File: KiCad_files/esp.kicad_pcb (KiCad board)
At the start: 2 copper layers, 86 x 75 mm, 69 parts, among them J1 Conn_01x02_Pin, J2 USB4105-GF-A, J3 Conn_01x16_Pin, Q2 DMP3099L, SW1 SLW-171175-7A-N-D, U1 B3U-1000P, U12 ESP32-S3-MINI-1U, U13 BNO085, U2 1060, U7 LTC4412xS6

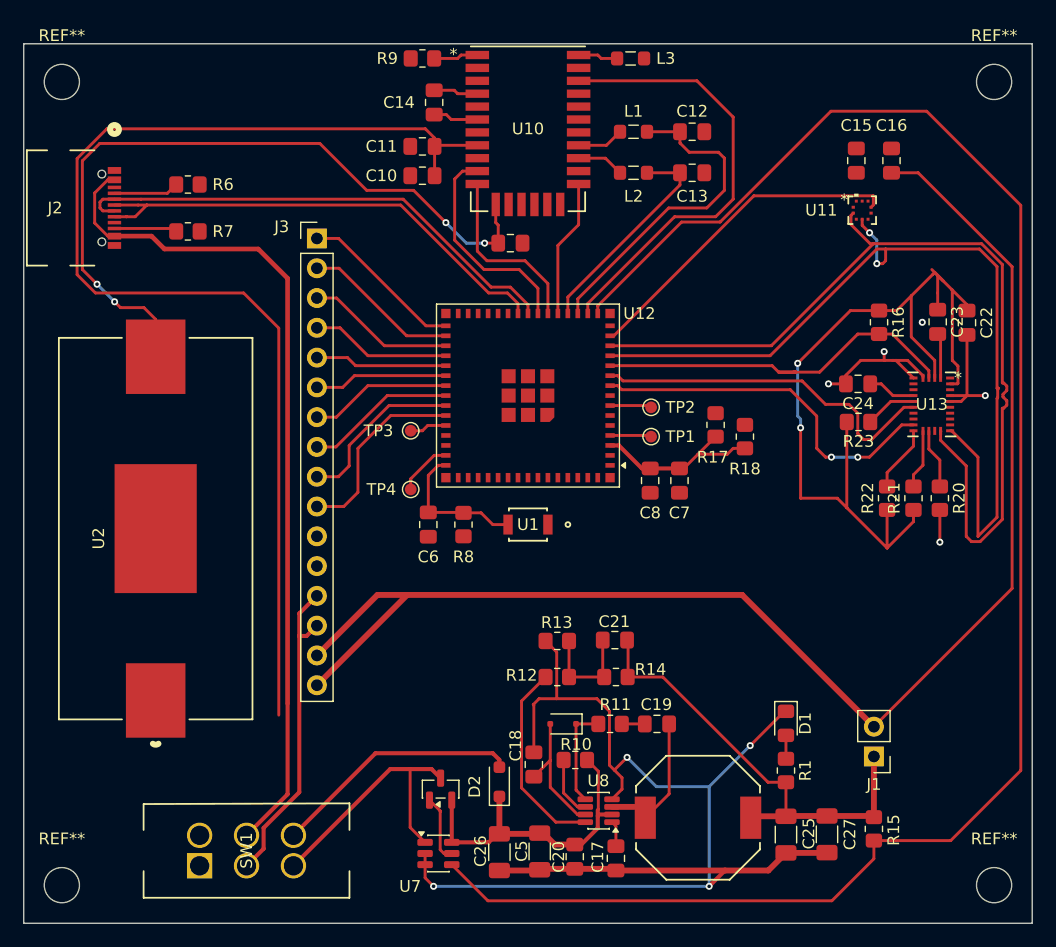
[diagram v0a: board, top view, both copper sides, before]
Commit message: backside GND fill
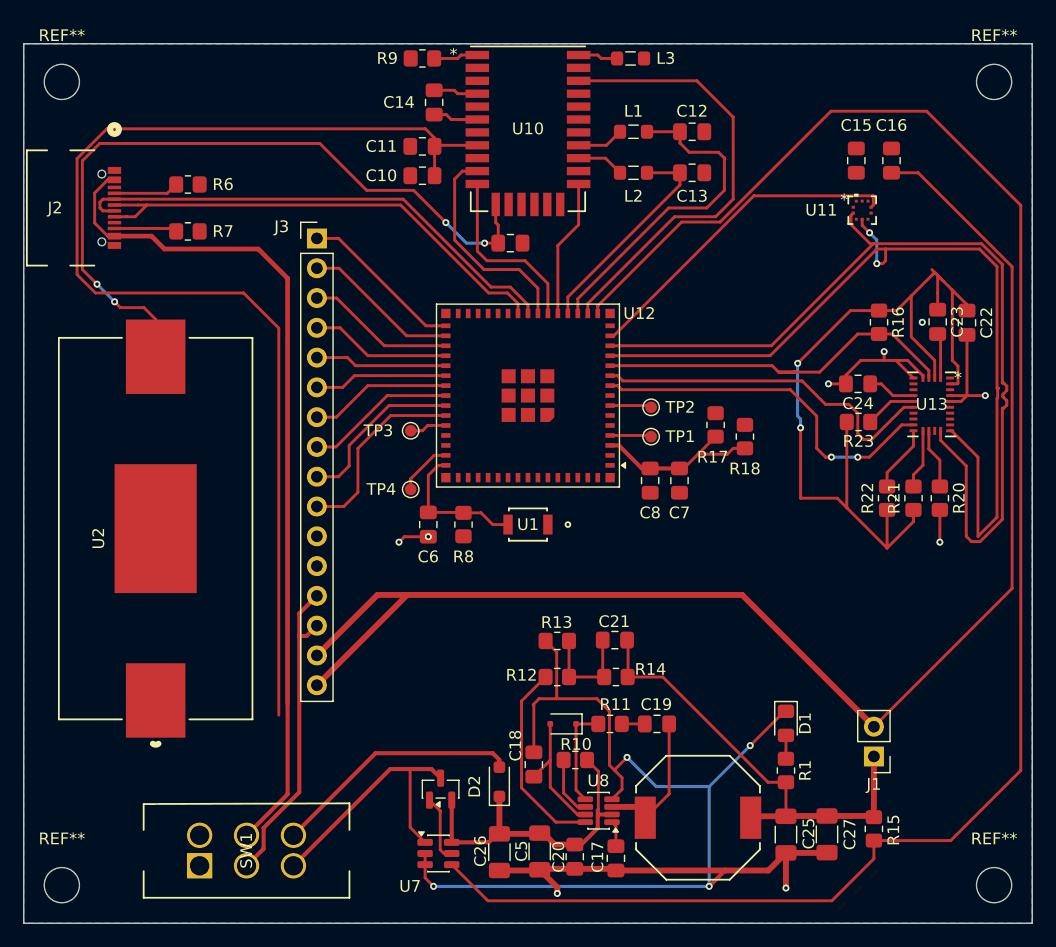
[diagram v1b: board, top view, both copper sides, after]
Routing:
- net GND: track 138.2 -> 146.5 mm, vias 9 -> 13
- added copper zone on B.Cu, net GND
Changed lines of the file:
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@@
 	)
 	(segment
+		(start 116.5 67.0375)
+		(end 114.4625 67.0375)
+		(width 0.25)
+		(layer "F.Cu")
+		(net 1)
+	)
+	(segment
 		(start 156.374999 52)
 		(end 157.874998 53.499999)
@@
 	)
 	(segment
+		(start 126 95.4375)
+		(end 127.5 96.9375)
+		(width 0.5)
+		(layer "F.Cu")
+		(net 1)
+	)
+	(segment
 		(start 127.45 80.85)
 		(end 125.95 80.85)
@@
 	)
 	(segment
+		(start 147 94)
+		(end 147 97)
+		(width 0.5)
+		(layer "F.Cu")
+		(net 1)
+	)
+	(segment
 		(start 125.45 81.35)
 		(end 125.5 81.4)
@@
 	)
 	(segment
+		(start 114.4625 67.0375)
+		(end 114 67.5)
+		(width 0.25)
+		(layer "F.Cu")
+		(net 1)
+	)
+	(segment
 		(start 132.5 95.5)
 		(end 141.8 95.5)
@@
 	)
 	(segment
+		(start 127.5 96.9375)
+		(end 127.5 97.45935)
+		(width 0.5)
+		(layer "F.Cu")
+		(net 1)
+	)
+	(segment
 		(start 147 94)
 		(end 150.475 94)
@@
 	)
 	(via
+		(at 127.5 97.45935)
+		(size 0.6)
+		(drill 0.3)
+		(layers "F.Cu" "B.Cu")
+		(net 1)
+	)
+	(via
 		(at 150.624998 54)
 		(size 0.6)
@@
 	)
 	(via
+		(at 114 67.5)
+		(size 0.6)
+		(drill 0.3)
+		(layers "F.Cu" "B.Cu")
+		(net 1)
+	)
+	(via
 		(at 143.95 84.85)
 		(size 0.6)
@@
 	)
 	(via
+		(at 116.5 67.0375)
+		(size 0.6)
+		(drill 0.3)
+		(layers "F.Cu" "B.Cu")
+		(net 1)
+	)
+	(via
+		(at 147 97)
+		(size 0.6)
+		(drill 0.3)
+		(layers "F.Cu" "B.Cu")
+		(net 1)
+	)
+	(via
 		(at 160.124998 67.5)
 		(size 0.6)
@@
 		(net 85)
 	)
+	(zone
+		(net 1)
+		(net_name "GND")
+		(layer "B.Cu")
+		(hatch edge 0.5)
+		(connect_pads
+			(clearance 0.5)
+		)
+		(min_thickness 0.25)
+		(filled_areas_thickness no)
+		(fill yes
+			(thermal_gap 0.5)
+			(thermal_bridge_width 0.5)
+		)
+		(polygon
+			(pts
+				(xy 168 100) (xy 82 100) (xy 82 25) (xy 168 25)
+			)
+		)
+	)
 	(group ""

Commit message: all connected for now
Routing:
- net +3.3V: track 315.1 -> 364.3 mm, vias 2 -> 4
- net GND: track 146.5 -> 192.0 mm, vias 13 -> 24
- net /I2C_CLK: track 78.2 -> 90.3 mm, vias 0 -> 2
- net /I2C_SDA: track 77.5 -> 85.5 mm, vias 2 -> 4
- net /BAROMETER_INT: track 28.5 -> 30.8 mm, vias 0 -> 2
- added copper zone on F.Cu, net GND

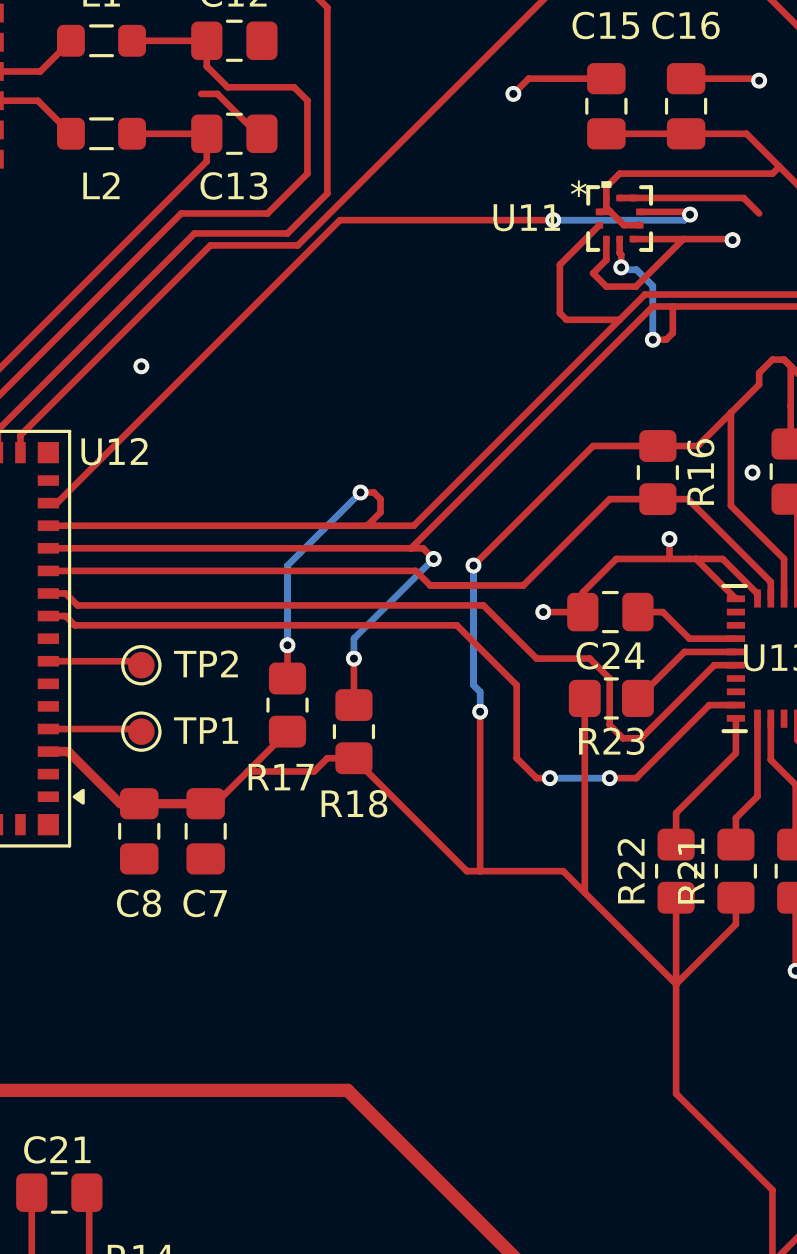
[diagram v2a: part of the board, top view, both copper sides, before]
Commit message: wider power trace for MCU
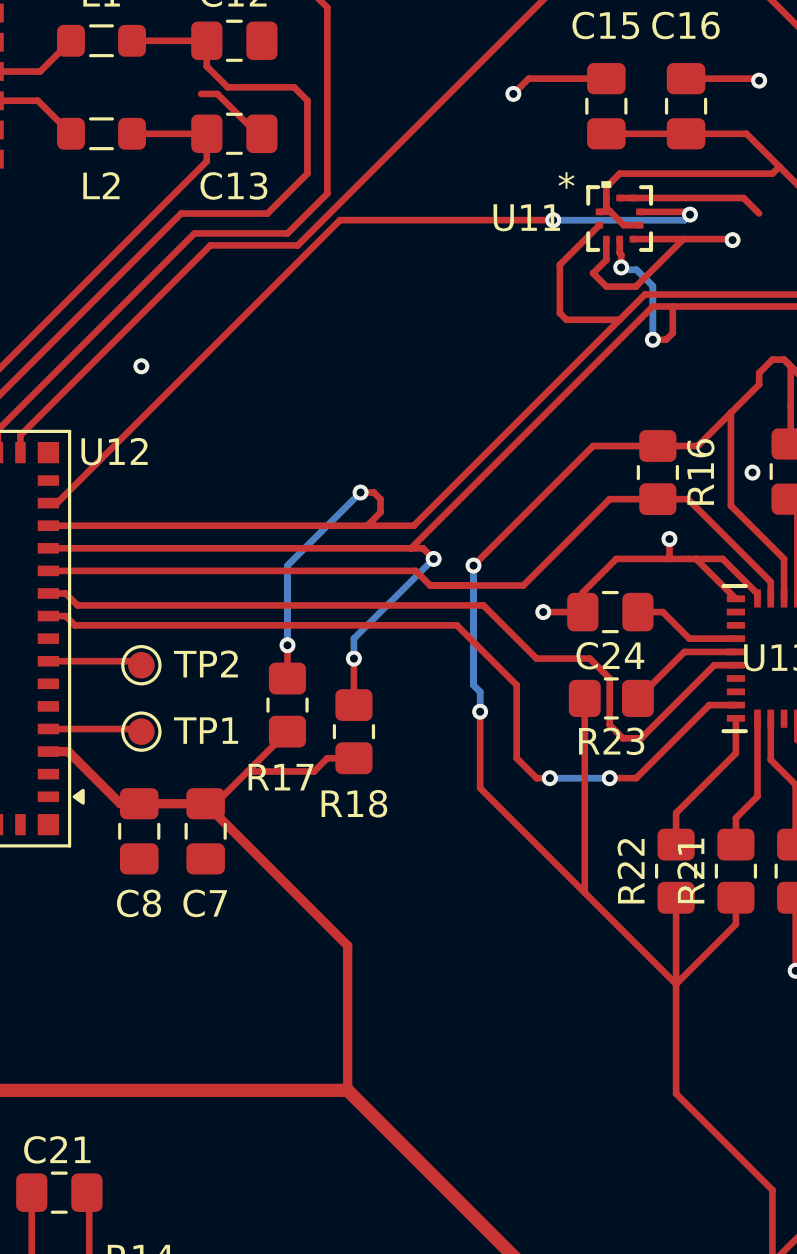
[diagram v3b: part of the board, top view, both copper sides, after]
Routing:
- net +3.3V: track 364.3 -> 369.0 mm
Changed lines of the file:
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@@
 		)
 		(fp_text user "*"
-			(at -1.535 -0.881 0)
+			(at -2.000001 -1.189499 0)
 			(layer "F.SilkS")
 			(effects
@@
 		)
 		(fp_text user "*"
-			(at -1.535 -0.881 0)
+			(at -2.000001 -1.189499 0)
 			(unlocked yes)
 			(layer "F.SilkS")
@@
 	)
 	(segment
+		(start 143.265 66.557468)
+		(end 143.265 72)
+		(width 0.35)
+		(layer "F.Cu")
+		(net 4)
+	)
+	(segment
 		(start 89.090538 32.25)
 		(end 86.549 34.791538)
@@
 		(start 152.5 47.75)
 		(end 148 52.25)
-		(width 0.25)
-		(layer "F.Cu")
-		(net 4)
-	)
-	(segment
-		(start 148.25 57.75)
-		(end 148.25 63.75)
 		(width 0.25)
 		(layer "F.Cu")
@@
 	)
 	(segment
-		(start 151.374998 63.75)
-		(end 152.187499 64.562501)
-		(width 0.25)
-		(layer "F.Cu")
-		(net 4)
-	)
-	(segment
 		(start 111.35 75.35)
 		(end 111.35 79.9)
@@
 	)
 	(segment
+		(start 152.187499 64.562501)
+		(end 148.25 60.625002)
+		(width 0.25)
+		(layer "F.Cu")
+		(net 4)
+	)
+	(segment
 		(start 154.260302 39.439499)
 		(end 153.6584 39.439499)
@@
 	)
 	(segment
+		(start 137.920032 61.2125)
+		(end 143.265 66.557468)
+		(width 0.35)
+		(layer "F.Cu")
+		(net 4)
+	)
+	(segment
 		(start 159.51281 37.23719)
 		(end 158.27562 36)
@@
 	)
 	(segment
+		(start 148.25 60.625002)
+		(end 148.25 57.75)
+		(width 0.25)
+		(layer "F.Cu")
+		(net 4)
+	)
+	(segment
 		(start 159.687499 53.4875)
 		(end 159.687499 52)
@@
 	)
 	(segment
-		(start 148.25 63.75)
-		(end 151.374998 63.75)
-		(width 0.25)
-		(layer "F.Cu")
-		(net 4)
-	)
-	(segment
 		(start 161.6689 53.952999)
 		(end 161.6689 52.481401)
@@
 	)
 	(segment
-		(start 148.25 63.75)
-		(end 147.75 63.75)
-		(width 0.25)
-		(layer "F.Cu")
-		(net 4)
-	)
-	(segment
 		(start 154.937499 47.75)
 		(end 156.437499 47.75)
@@
 		(width 0.25)
 		(layer "F.Cu")
-		(net 4)
-	)
-	(segment
-		(start 147.75 63.75)
-		(end 143.5 59.5)
-		(width 0.25)
-		(layer "F.Cu")

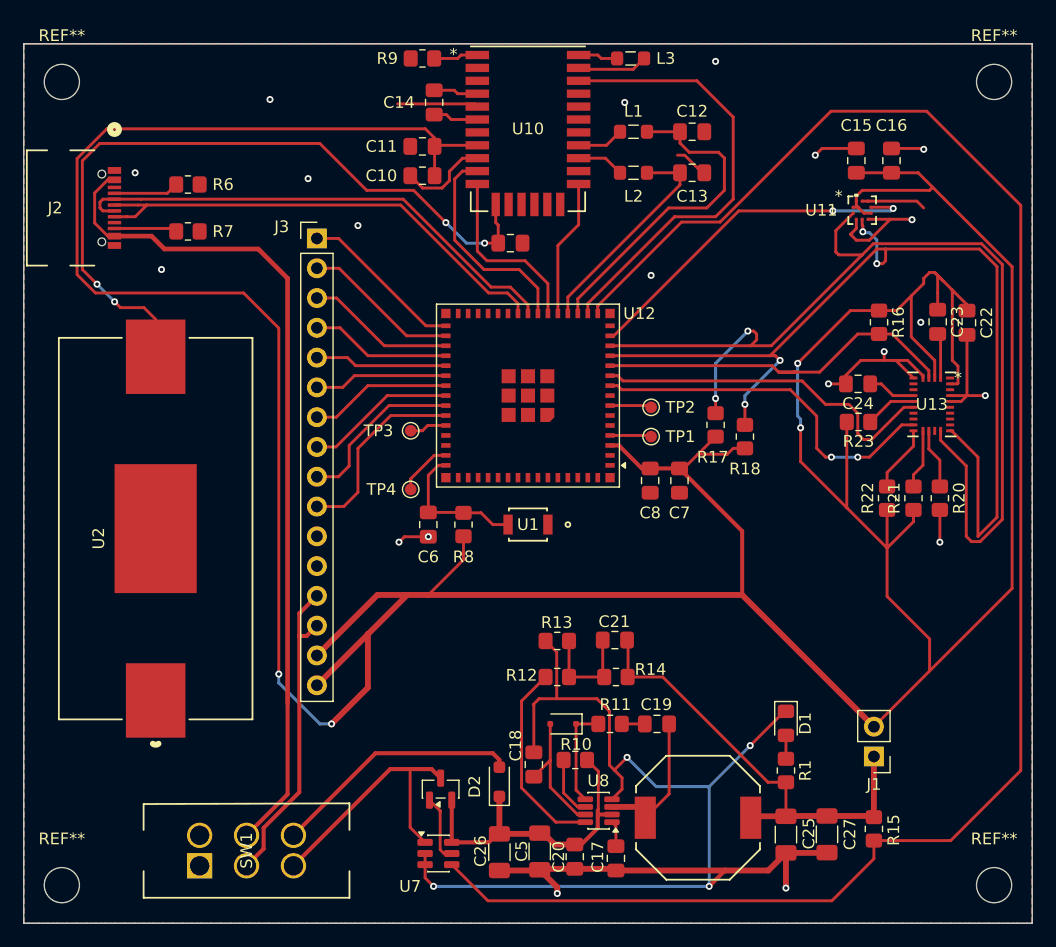
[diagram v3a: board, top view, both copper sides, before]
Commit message: copper fillin minimietäisyys laskettu vastaamaan valmistajan speksiä, vioja yms
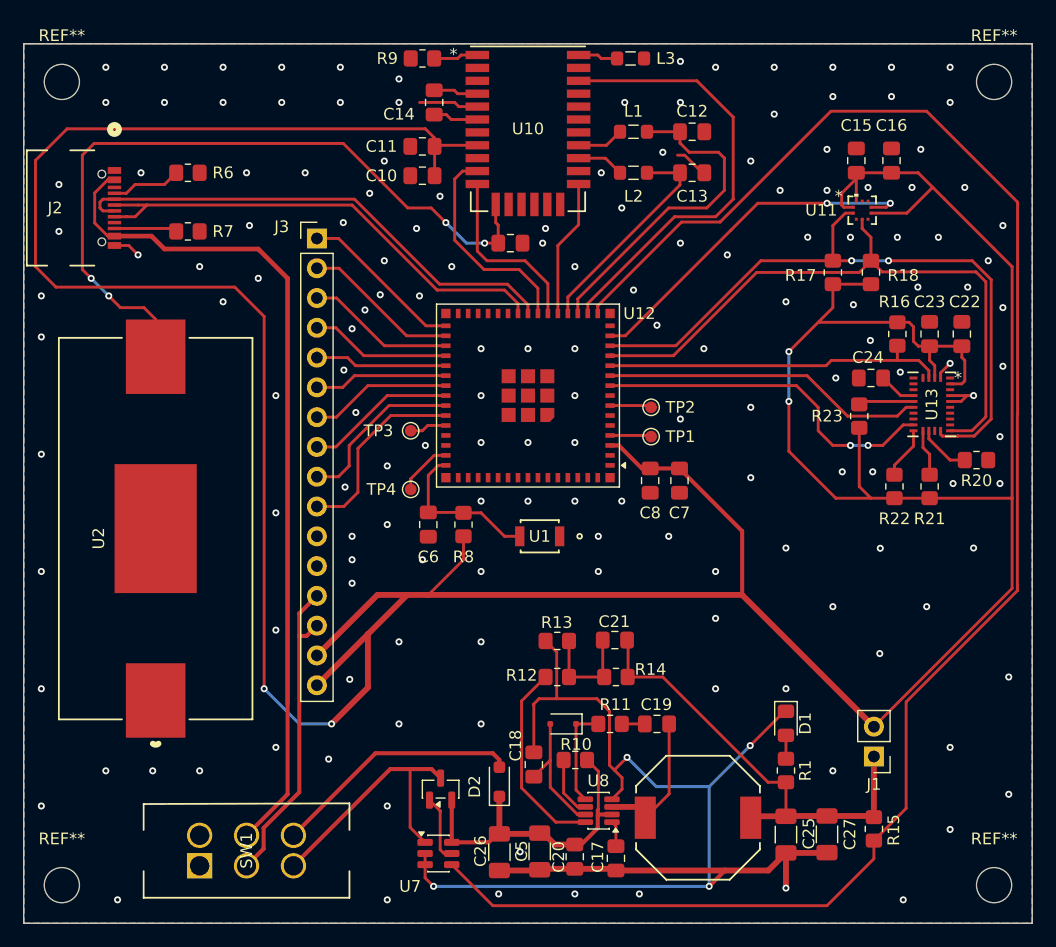
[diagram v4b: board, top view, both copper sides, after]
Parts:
- moved R18 17.7 mm to (154.2, 44.5)
- moved R17 16.4 mm to (151.0, 44.5)
- moved R20 4.51 mm to (163.2, 60.5), turned to 0 degrees
- moved R16 1.86 mm to (156.5, 49.8)
- moved R21 1.70 mm to (159.2, 62.8)
- moved U1 1.41 mm to (126.0, 67.0)
- moved C23 1.24 mm to (159.2, 49.8), turned to 90 degrees
- moved C24 1.21 mm to (154.2, 53.5)
- moved R22 1.18 mm to (156.2, 62.8)
- moved C22 1.06 mm to (162.0, 49.8), turned to 90 degrees
- moved R6 1.00 mm to (96.0, 36.0)
- moved R23 0.50 mm to (153.2, 56.8), turned to -90 degrees
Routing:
- net GND: track 192.0 -> 128.2 mm, vias 24 -> 162
- net /I2C_CLK: track 90.3 -> 58.5 mm
- net /I2C_SDA: track 85.5 -> 55.2 mm, vias 4 -> 0
- net +3.3V: track 369.0 -> 352.9 mm
- net /BAT_STAT: track 150.4 -> 146.7 mm
- net /IMU_BOOTN: track 32.4 -> 29.6 mm
- net /IMU_NRST: track 30.3 -> 27.6 mm
- net Net-(U12-EN): track 12.2 -> 13.7 mm
- net /IMU_INT: track 31.2 -> 29.9 mm
- net Net-(U13-ENV_SCL): track 5.68 -> 4.42 mm
- net Net-(U13-ENV_SDA): track 5.07 -> 3.97 mm
- net Net-(U13-CAP): track 4.10 -> 3.21 mm
- net Net-(U13-SA0/H_MOSI): track 5.13 -> 4.49 mm

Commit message: siivoilua
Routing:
- net GND: track 128.2 -> 32.6 mm, vias 162 -> 164
- net /BAT_STAT: track 146.7 -> 145.9 mm
- net /BAT: track 27.4 -> 28.0 mm

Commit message: gerberit
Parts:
- moved C22 0.25 mm to (162.2, 49.8)
- moved C23 0.25 mm to (159.5, 49.8)
- moved R16 0.25 mm to (156.8, 49.8)
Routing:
- net GND: track 32.6 -> 1.09 mm, vias 164 -> 168
